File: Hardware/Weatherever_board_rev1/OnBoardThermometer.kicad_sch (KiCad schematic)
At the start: 3 parts, among them U501 LM75B

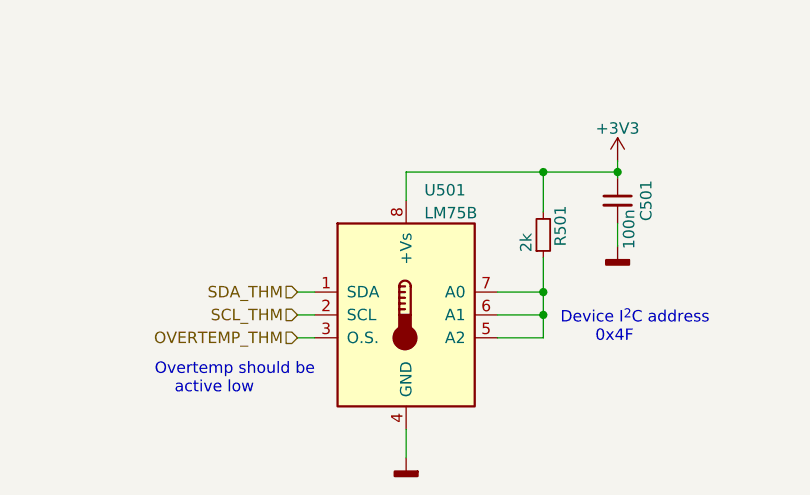
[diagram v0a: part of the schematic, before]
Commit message: New hw element and CommHandler tests
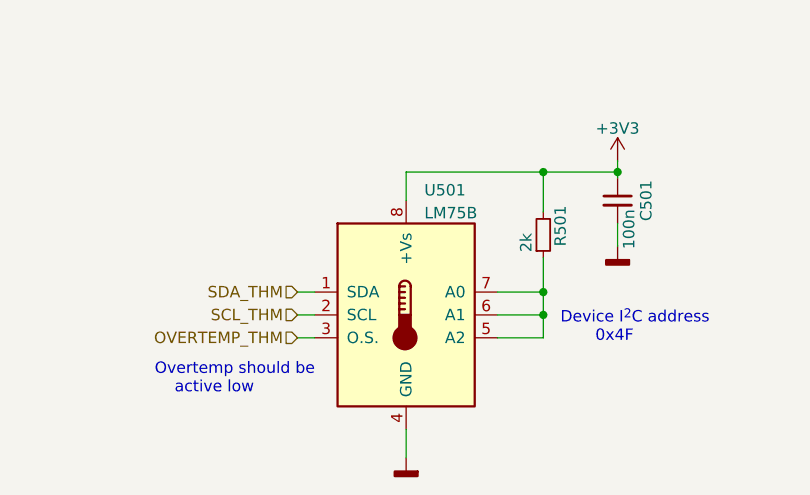
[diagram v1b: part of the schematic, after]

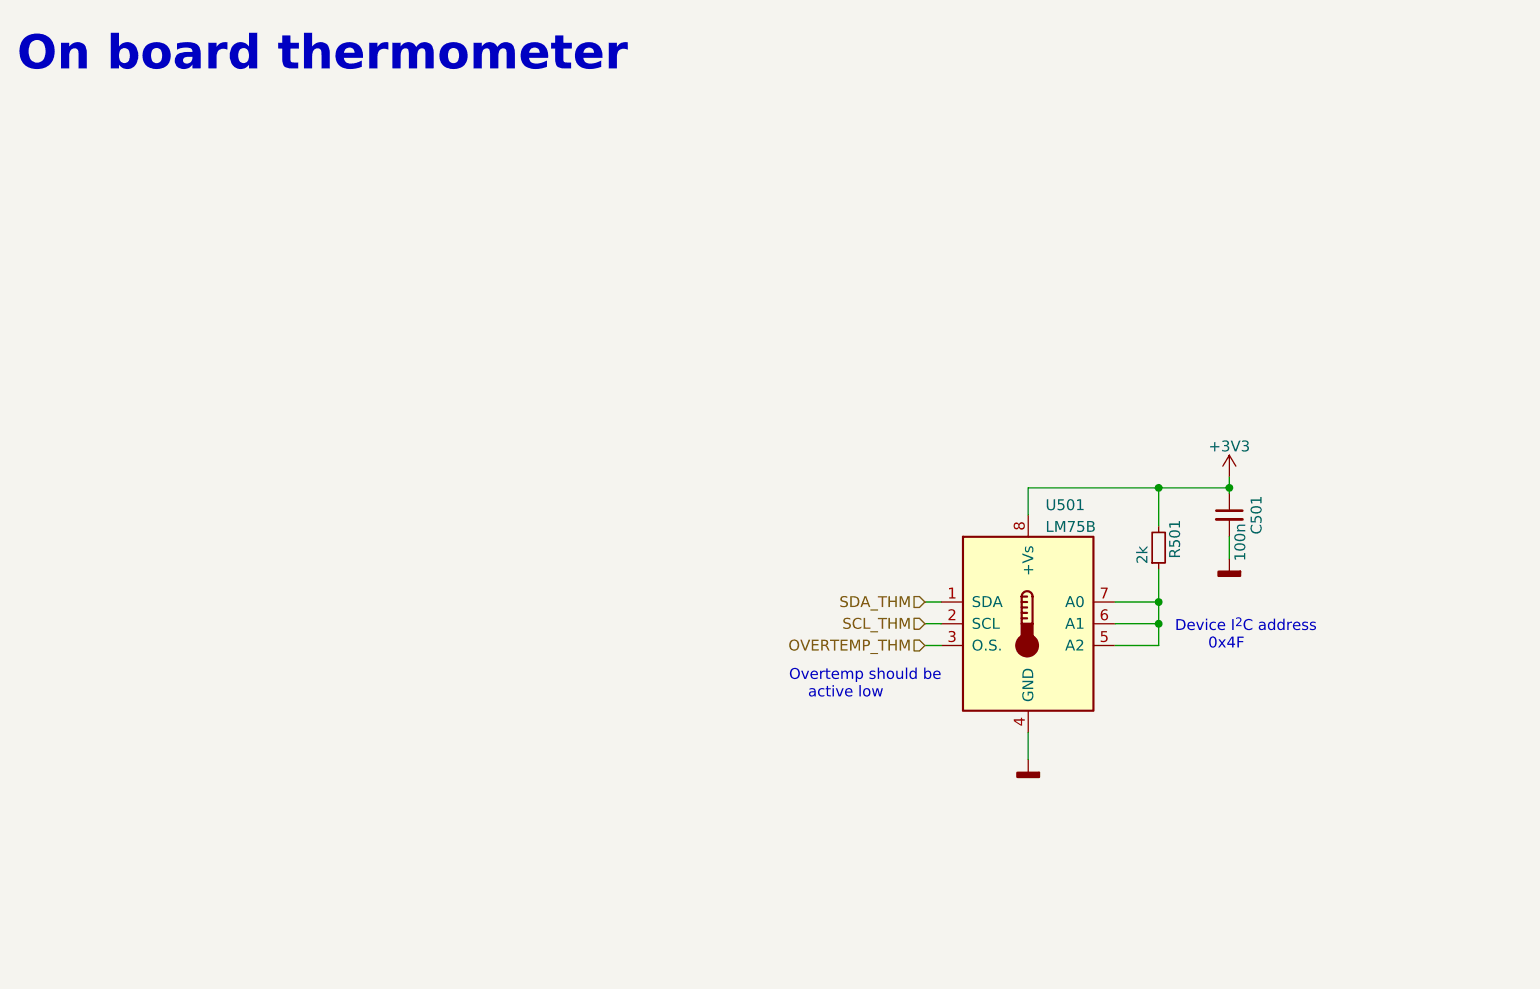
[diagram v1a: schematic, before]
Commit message: Funished schematics and GPIO drv interface
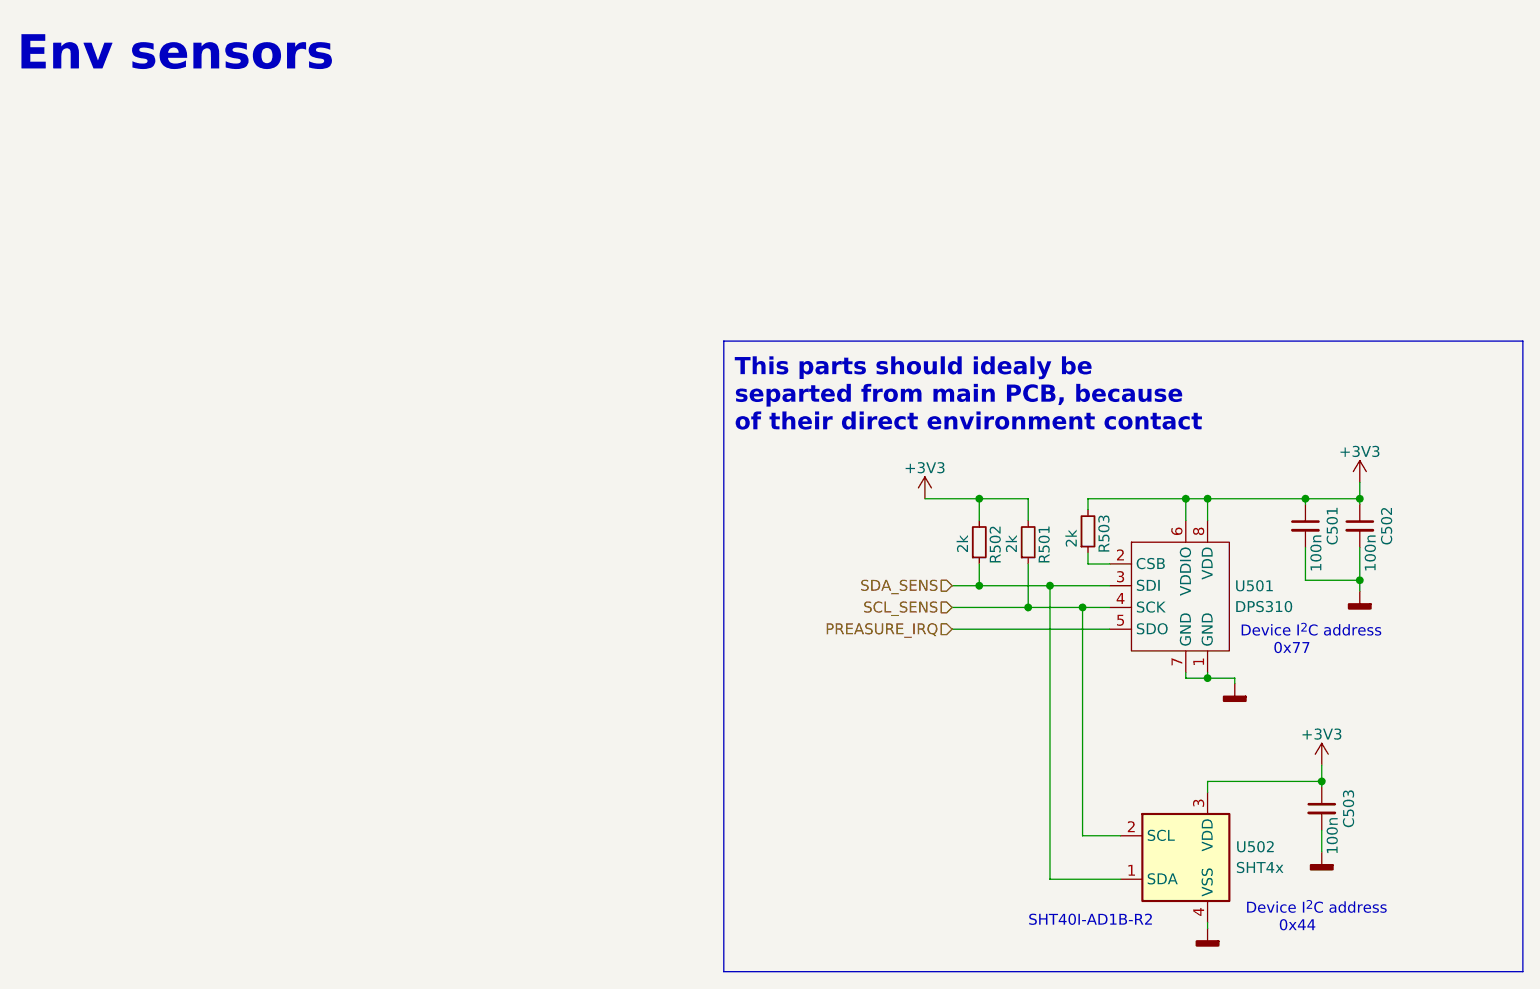
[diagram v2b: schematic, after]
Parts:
- removed U501: LM75B, symbol Sensor_Temperature:LM75B
- added C502, C503: 100n, Capacitor_SMD:C_0805_2012Metric_Pad1.18x1.45mm_HandSolder, symbol Device:C_Small
- added R502, R503: 2k, Resistor_SMD:R_0805_2012Metric_Pad1.20x1.40mm_HandSolder, symbol Device:R_Small
- added U501: DPS310, Package_LGA:Bosch_LGA-8_2x2.5mm_P0.65mm_ClockwisePinNumbering, symbol CustomSymbols:DPS310
- added U502: SHT4x, Sensor_Humidity:Sensirion_DFN-4_1.5x1.5mm_P0.8mm_SHT4x_NoCentralPad, symbol Sensor_Humidity:SHT4x
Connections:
- net +3V3: now also C502.1, C503.1, R502.2, R503.2, U501.6 (VDDIO), U501.8 (VDD), U502.3 (VDD)
- net GNDD: now also C502.2, C503.2, U501.1 (GND), U501.7 (GND), U502.4 (VSS)
- net SCL_SENS: now reaches R501.1
- net SCL_SENS: now also U501.4 (SCK), U502.2 (SCL)
- new net: R503.1, U501.2 (CSB)
- new net PREASURE_IRQ: U501.5 (SDO)
- new net SDA_SENS: R502.1, U501.3 (SDI), U502.1 (SDA)
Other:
- note added: "Device I^{2}C address 0x44"
- note added: "Device I^{2}C address 0x77"
- note added: "Env sensors"
- note added: "SHT40I-AD1B-R2"
- note added: "This parts should idealy be separted from main PCB, because of their direct environment contact"
- note removed: "Device I^{2}C address 0x4F"
- note removed: "On board thermometer"
- note removed: "Overtemp should be active low"
- moved on the sheet: C501
